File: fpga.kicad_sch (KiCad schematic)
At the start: 32 parts, among them J301 program, U301 ICE40HX8K-BG121, U302 W25Q32JVSS, Y301 50Mhz, Y302 12Mhz

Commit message: Working on board layout
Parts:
- D301: footprint LED_SMD:LED_1210_3225Metric -> LED_SMD:LED_1206_3216Metric
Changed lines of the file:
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@@
 			)
 		)
-		(property "Footprint" "LED_SMD:LED_1210_3225Metric"
+		(property "Footprint" "LED_SMD:LED_1206_3216Metric"
 			(at 210.82 66.04 0)
 			(effects

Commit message: More board layout
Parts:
- C301, C302, C303, C304, C305, C306, C307, C308, C309, C310, C311, C312, C313, C314, C315, C316, C317, C318: footprint Capacitor_SMD:C_0805_2012Metric -> Capacitor_SMD:C_0603_1608Metric
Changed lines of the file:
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@@
 			)
 		)
-		(property "Footprint" "Capacitor_SMD:C_0805_2012Metric"
+		(property "Footprint" "Capacitor_SMD:C_0603_1608Metric"
 			(at 40.9448 173.99 0)
 			(effects
@@
 			)
 		)
-		(property "Footprint" "Capacitor_SMD:C_0805_2012Metric"
+		(property "Footprint" "Capacitor_SMD:C_0603_1608Metric"
 			(at 240.3348 146.05 0)
 			(effects
@@
 			)
 		)
-		(property "Footprint" "Capacitor_SMD:C_0805_2012Metric"
+		(property "Footprint" "Capacitor_SMD:C_0603_1608Metric"
 			(at 193.3448 146.05 0)
 			(effects
@@
 			)
 		)
-		(property "Footprint" "Capacitor_SMD:C_0805_2012Metric"
+		(property "Footprint" "Capacitor_SMD:C_0603_1608Metric"
 			(at 72.6948 34.29 0)
 			(effects
@@
 			)
 		)
-		(property "Footprint" "Capacitor_SMD:C_0805_2012Metric"
+		(property "Footprint" "Capacitor_SMD:C_0603_1608Metric"
 			(at 100.6348 148.59 0)
 			(effects
@@
 			)
 		)
-		(property "Footprint" "Capacitor_SMD:C_0805_2012Metric"
+		(property "Footprint" "Capacitor_SMD:C_0603_1608Metric"
 			(at 108.2548 148.59 0)
 			(effects
@@
 			)
 		)
-		(property "Footprint" "Capacitor_SMD:C_0805_2012Metric"
+		(property "Footprint" "Capacitor_SMD:C_0603_1608Metric"
 			(at 216.2048 27.94 0)
 			(effects
@@
 			)
 		)
-		(property "Footprint" "Capacitor_SMD:C_0805_2012Metric"
+		(property "Footprint" "Capacitor_SMD:C_0603_1608Metric"
 			(at 208.5848 27.94 0)
 			(effects
@@
 			)
 		)
-		(property "Footprint" "Capacitor_SMD:C_0805_2012Metric"
+		(property "Footprint" "Capacitor_SMD:C_0603_1608Metric"
 			(at 80.3148 34.29 0)
 			(effects
@@
 			)
 		)
-		(property "Footprint" "Capacitor_SMD:C_0805_2012Metric"
+		(property "Footprint" "Capacitor_SMD:C_0603_1608Metric"
 			(at 132.3848 34.29 0)
 			(effects
@@
 			)
 		)
-		(property "Footprint" "Capacitor_SMD:C_0805_2012Metric"
+		(property "Footprint" "Capacitor_SMD:C_0603_1608Metric"
 			(at 273.3548 34.29 0)
 			(effects
@@
 			)
 		)
-		(property "Footprint" "Capacitor_SMD:C_0805_2012Metric"
+		(property "Footprint" "Capacitor_SMD:C_0603_1608Metric"
 			(at 48.5648 140.97 0)
 			(effects
@@
 			)
 		)
-		(property "Footprint" "Capacitor_SMD:C_0805_2012Metric"
+		(property "Footprint" "Capacitor_SMD:C_0603_1608Metric"
 			(at 168.6052 173.99 0)
 			(effects
@@
 			)
 		)
-		(property "Footprint" "Capacitor_SMD:C_0805_2012Metric"
+		(property "Footprint" "Capacitor_SMD:C_0603_1608Metric"
 			(at 40.9448 140.97 0)
 			(effects
@@
 			)
 		)
-		(property "Footprint" "Capacitor_SMD:C_0805_2012Metric"
+		(property "Footprint" "Capacitor_SMD:C_0603_1608Metric"
 			(at 48.5648 173.99 0)
 			(effects
@@
 			)
 		)
-		(property "Footprint" "Capacitor_SMD:C_0805_2012Metric"
+		(property "Footprint" "Capacitor_SMD:C_0603_1608Metric"
 			(at 93.0148 148.59 0)
 			(effects
@@
 			)
 		)
-		(property "Footprint" "Capacitor_SMD:C_0805_2012Metric"
+		(property "Footprint" "Capacitor_SMD:C_0603_1608Metric"
 			(at 280.9748 34.29 0)
 			(effects
@@
 			)
 		)
-		(property "Footprint" "Capacitor_SMD:C_0805_2012Metric"
+		(property "Footprint" "Capacitor_SMD:C_0603_1608Metric"
 			(at 140.0048 34.29 0)
 			(effects

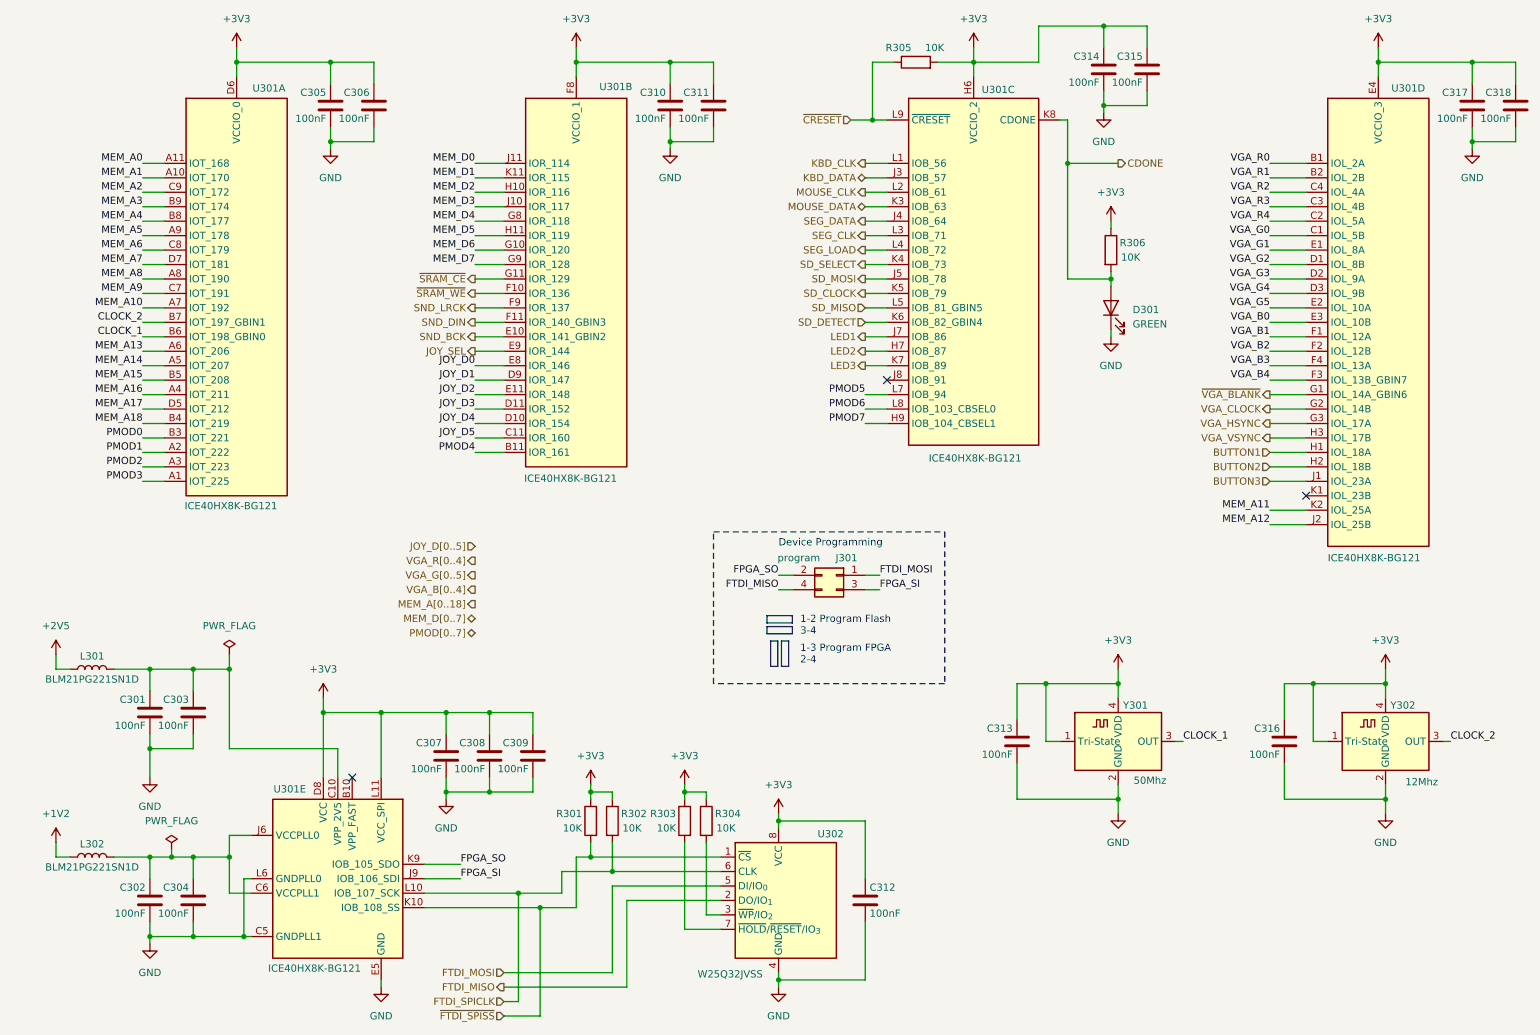
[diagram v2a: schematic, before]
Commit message: Started FPGA fanout
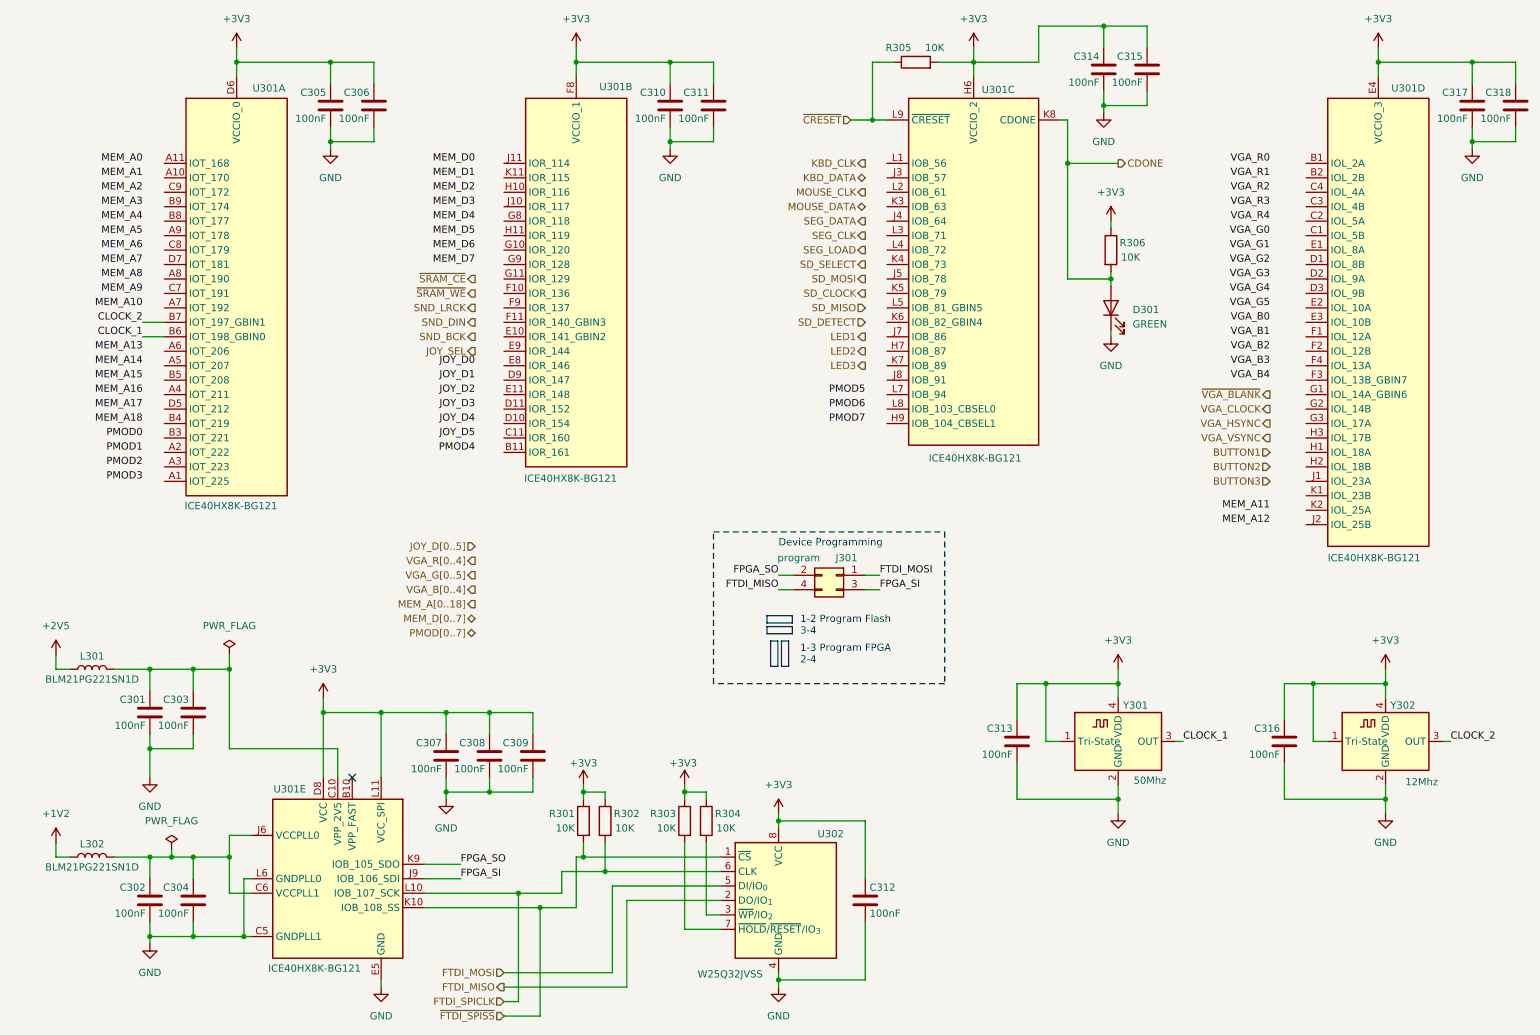
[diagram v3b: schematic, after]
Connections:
- net BUTTON1: no longer U301.H1 (IOL_18A)
- net BUTTON2: no longer U301.H2 (IOL_18B)
- net BUTTON3: no longer U301.J1 (IOL_23A)
- net JOY_D0: no longer U301.E8 (IOR_146)
- net JOY_D1: no longer U301.D9 (IOR_147)
- net JOY_D2: no longer U301.E11 (IOR_148)
- net JOY_D3: no longer U301.D11 (IOR_152)
- net JOY_D4: no longer U301.D10 (IOR_154)
- net JOY_D5: no longer U301.C11 (IOR_160)
- net JOY_SEL: no longer U301.E9 (IOR_144)
- net KBD_CLK: no longer U301.L1 (IOB_56)
- net KBD_DATA: no longer U301.J3 (IOB_57)
- net LED1: no longer U301.J7 (IOB_86)
- net LED2: no longer U301.H7 (IOB_87)
- net LED3: no longer U301.K7 (IOB_89)
- net MEM_A0: no longer U301.A11 (IOT_168)
- net MEM_A1: no longer U301.A10 (IOT_170)
- net MEM_A10: no longer U301.A7 (IOT_192)
- net MEM_A11: no longer U301.K2 (IOL_25A)
- net MEM_A12: no longer U301.J2 (IOL_25B)
- net MEM_A13: no longer U301.A6 (IOT_206)
- net MEM_A14: no longer U301.A5 (IOT_207)
- net MEM_A15: no longer U301.B5 (IOT_208)
- net MEM_A16: no longer U301.A4 (IOT_211)
- net MEM_A17: no longer U301.D5 (IOT_212)
- net MEM_A18: no longer U301.B4 (IOT_219)
- net MEM_A2: no longer U301.C9 (IOT_172)
- net MEM_A3: no longer U301.B9 (IOT_174)
- net MEM_A4: no longer U301.B8 (IOT_177)
- net MEM_A5: no longer U301.A9 (IOT_178)
- net MEM_A6: no longer U301.C8 (IOT_179)
- net MEM_A7: no longer U301.D7 (IOT_181)
- net MEM_A8: no longer U301.A8 (IOT_190)
- net MEM_A9: no longer U301.C7 (IOT_191)
- net MEM_D0: no longer U301.J11 (IOR_114)
- net MEM_D1: no longer U301.K11 (IOR_115)
- net MEM_D2: no longer U301.H10 (IOR_116)
- net MEM_D3: no longer U301.J10 (IOR_117)
- net MEM_D4: no longer U301.G8 (IOR_118)
- net MEM_D5: no longer U301.H11 (IOR_119)
- net MEM_D6: no longer U301.G10 (IOR_120)
- net MEM_D7: no longer U301.G9 (IOR_128)
- net MOUSE_CLK: no longer U301.L2 (IOB_61)
- net MOUSE_DATA: no longer U301.K3 (IOB_63)
- net PMOD0: no longer U301.B3 (IOT_221)
- net PMOD1: no longer U301.A2 (IOT_222)
- net PMOD2: no longer U301.A3 (IOT_223)
- net PMOD3: no longer U301.A1 (IOT_225)
- net PMOD4: no longer U301.B11 (IOR_161)
- net PMOD5: no longer U301.L7 (IOB_94)
- net PMOD6: no longer U301.L8 (IOB_103_CBSEL0)
- net PMOD7: no longer U301.H9 (IOB_104_CBSEL1)
- net SD_CLOCK: no longer U301.K5 (IOB_79)
- net SD_DETECT: no longer U301.K6 (IOB_82_GBIN4)
- net SD_MISO: no longer U301.L5 (IOB_81_GBIN5)
- net SD_MOSI: no longer U301.J5 (IOB_78)
- net SD_SELECT: no longer U301.K4 (IOB_73)
- net SEG_CLK: no longer U301.L3 (IOB_71)
- net SEG_DATA: no longer U301.J4 (IOB_64)
- net SEG_LOAD: no longer U301.L4 (IOB_72)
- net SND_BCK: no longer U301.E10 (IOR_141_GBIN2)
- net SND_DIN: no longer U301.F11 (IOR_140_GBIN3)
- net SND_LRCK: no longer U301.F9 (IOR_137)
- net VGA_B0: no longer U301.E3 (IOL_10B)
- net VGA_B1: no longer U301.F1 (IOL_12A)
- net VGA_B2: no longer U301.F2 (IOL_12B)
- net VGA_B3: no longer U301.F4 (IOL_13A)
- net VGA_B4: no longer U301.F3 (IOL_13B_GBIN7)
- net VGA_CLOCK: no longer U301.G2 (IOL_14B)
- net VGA_G0: no longer U301.C1 (IOL_5B)
- net VGA_G1: no longer U301.E1 (IOL_8A)
- net VGA_G2: no longer U301.D1 (IOL_8B)
- net VGA_G3: no longer U301.D2 (IOL_9A)
- net VGA_G4: no longer U301.D3 (IOL_9B)
- net VGA_G5: no longer U301.E2 (IOL_10A)
- net VGA_HSYNC: no longer U301.G3 (IOL_17A)
- net VGA_R0: no longer U301.B1 (IOL_2A)
- net VGA_R1: no longer U301.B2 (IOL_2B)
- net VGA_R2: no longer U301.C4 (IOL_4A)
- net VGA_R3: no longer U301.C3 (IOL_4B)
- net VGA_R4: no longer U301.C2 (IOL_5A)
- net VGA_VSYNC: no longer U301.H3 (IOL_17B)
- net ~{SRAM_CE}: no longer U301.G11 (IOR_129)
- net ~{SRAM_WE}: no longer U301.F10 (IOR_136)
- net ~{VGA_BLANK}: no longer U301.G1 (IOL_14A_GBIN6)
- no-connect marks 3 -> 1
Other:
- moved on the sheet: R301, R302

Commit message: Initial FPGA layout done
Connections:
- net BUTTON1: now also U301.K5 (IOB_79)
- net BUTTON2: now also U301.L5 (IOB_81_GBIN5)
- net BUTTON3: now also U301.K6 (IOB_82_GBIN4)
- net JOY_D0: now also U301.A6 (IOT_206)
- net JOY_D1: now also U301.A7 (IOT_192)
- net JOY_D2: now also U301.D7 (IOT_181)
- net JOY_D3: now also U301.B8 (IOT_177)
- net JOY_D4: now also U301.A8 (IOT_190)
- net JOY_D5: now also U301.C7 (IOT_191)
- net JOY_SEL: now also U301.A5 (IOT_207)
- net KBD_CLK: now also U301.A9 (IOT_178)
- net KBD_DATA: now also U301.B9 (IOT_174)
- net LED1: now also U301.L4 (IOB_72)
- net LED2: now also U301.K4 (IOB_73)
- net LED3: now also U301.J5 (IOB_78)
- net MEM_A0: now also U301.L2 (IOB_61)
- net MEM_A1: now also U301.L1 (IOB_56)
- net MEM_A10: now also U301.A1 (IOT_225)
- net MEM_A11: now also U301.A2 (IOT_222)
- net MEM_A12: now also U301.B2 (IOL_2B)
- net MEM_A13: now also U301.B1 (IOL_2A)
- net MEM_A14: now also U301.C2 (IOL_5A)
- net MEM_A15: now also U301.E2 (IOL_10A)
- net MEM_A16: now also U301.E3 (IOL_10B)
- net MEM_A17: now also U301.E1 (IOL_8A)
- net MEM_A18: now also U301.F3 (IOL_13B_GBIN7)
- net MEM_A2: now also U301.K2 (IOL_25A)
- net MEM_A3: now also U301.K1 (IOL_23B)
- net MEM_A4: now also U301.J2 (IOL_25B)
- net MEM_A5: now also U301.G2 (IOL_14B)
- net MEM_A6: now also U301.G3 (IOL_17A)
- net MEM_A7: now also U301.F1 (IOL_12A)
- net MEM_A8: now also U301.F4 (IOL_13A)
- net MEM_A9: now also U301.F2 (IOL_12B)
- net MEM_D0: now also U301.J3 (IOB_57)
- net MEM_D1: now also U301.H1 (IOL_18A)
- net MEM_D2: now also U301.H2 (IOL_18B)
- net MEM_D3: now also U301.H3 (IOL_17B)
- net MEM_D4: now also U301.C1 (IOL_5B)
- net MEM_D5: now also U301.D2 (IOL_9A)
- net MEM_D6: now also U301.D3 (IOL_9B)
- net MEM_D7: now also U301.D1 (IOL_8B)
- net MOUSE_CLK: now also U301.C9 (IOT_172)
- net MOUSE_DATA: now also U301.A10 (IOT_170)
- net PMOD0: now also U301.B5 (IOT_208)
- net PMOD1: now also U301.A4 (IOT_211)
- net PMOD2: now also U301.C4 (IOL_4A)
- net PMOD3: now also U301.B3 (IOT_221)
- net PMOD4: now also U301.D5 (IOT_212)
- net PMOD5: now also U301.B4 (IOT_219)
- net PMOD6: now also U301.A3 (IOT_223)
- net PMOD7: now also U301.C3 (IOL_4B)
- net SD_CLOCK: now also U301.C11 (IOR_160)
- net SD_DETECT: now also U301.D9 (IOR_147)
- net SD_MISO: now also U301.D10 (IOR_154)
- net SD_MOSI: now also U301.B11 (IOR_161)
- net SD_SELECT: now also U301.A11 (IOT_168)
- net SEG_CLK: now also U301.J4 (IOB_64)
- net SEG_DATA: now also U301.K3 (IOB_63)
- net SEG_LOAD: now also U301.L3 (IOB_71)
- net SND_BCK: now also U301.D11 (IOR_152)
- net SND_DIN: now also U301.E9 (IOR_144)
- net SND_LRCK: now also U301.E10 (IOR_141_GBIN2)
- net VGA_B0: now also U301.H10 (IOR_116)
- net VGA_B1: now also U301.J11 (IOR_114)
- net VGA_B2: now also U301.H9 (IOB_104_CBSEL1)
- net VGA_B3: now also U301.K11 (IOR_115)
- net VGA_B4: now also U301.J10 (IOR_117)
- net VGA_CLOCK: now also U301.F11 (IOR_140_GBIN3)
- net VGA_G0: now also U301.K7 (IOB_89)
- net VGA_G1: now also U301.J7 (IOB_86)
- net VGA_G2: now also U301.L7 (IOB_94)
- net VGA_G3: now also U301.H7 (IOB_87)
- net VGA_G4: now also U301.L8 (IOB_103_CBSEL0)
- net VGA_G5: now also U301.J8 (IOB_91)
- net VGA_HSYNC: now also U301.F10 (IOR_136)
- net VGA_R0: now also U301.G10 (IOR_120)
- net VGA_R1: now also U301.G11 (IOR_129)
- net VGA_R2: now also U301.E8 (IOR_146)
- net VGA_R3: now also U301.G8 (IOR_118)
- net VGA_R4: now also U301.H11 (IOR_119)
- net VGA_VSYNC: now also U301.F9 (IOR_137)
- net ~{SRAM_CE}: now also U301.J1 (IOL_23A)
- net ~{SRAM_WE}: now also U301.G1 (IOL_14A_GBIN6)
- net ~{VGA_BLANK}: now also U301.E11 (IOR_148)

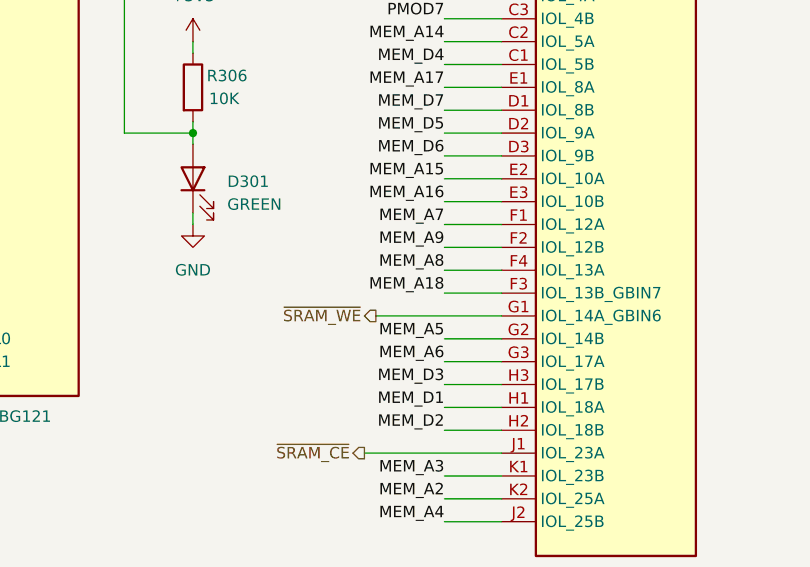
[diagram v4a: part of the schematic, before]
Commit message: Started board routing
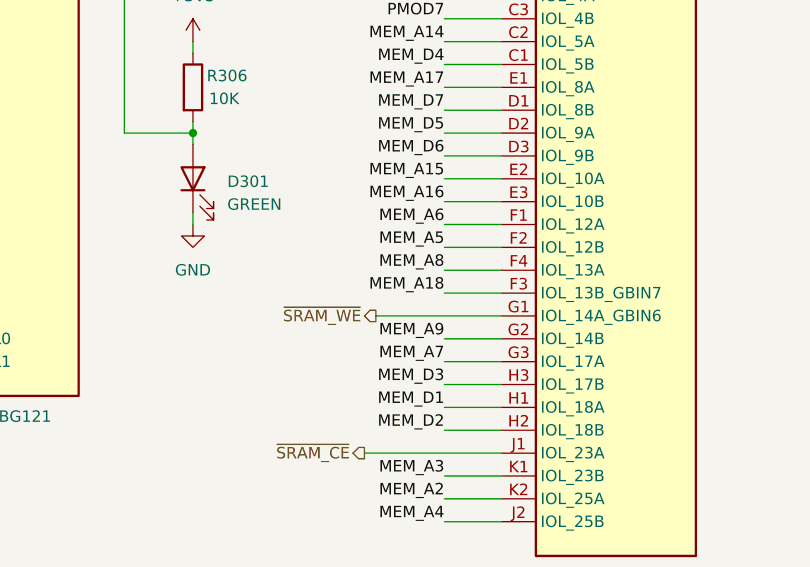
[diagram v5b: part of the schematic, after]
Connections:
- net MEM_A5: now also U301.F2 (IOL_12B); no longer U301.G2 (IOL_14B)
- net MEM_A6: now also U301.F1 (IOL_12A); no longer U301.G3 (IOL_17A)
- net MEM_A7: now also U301.G3 (IOL_17A); no longer U301.F1 (IOL_12A)
- net MEM_A9: now also U301.G2 (IOL_14B); no longer U301.F2 (IOL_12B)
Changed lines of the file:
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@@
 	)
 	(label "MEM_A7"
-		(at 238.76 71.12 180)
+		(at 238.76 86.36 180)
 		(effects
 			(font
@@
 	)
 	(label "MEM_A6"
-		(at 238.76 86.36 180)
+		(at 238.76 71.12 180)
 		(effects
 			(font
@@
 	)
 	(label "MEM_A5"
-		(at 238.76 83.82 180)
+		(at 238.76 73.66 180)
 		(effects
 			(font
@@
 	)
 	(label "MEM_A9"
-		(at 238.76 73.66 180)
-		(effects
-			(font
+		(at 238.76 83.82 180)
+		(effects
+			(font

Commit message: Routed SRAM
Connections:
- net MEM_A10: now also U301.A2 (IOT_222); no longer U301.A1 (IOT_225)
- net MEM_A11: now also U301.A1 (IOT_225); no longer U301.A2 (IOT_222)
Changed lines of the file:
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@@
 	)
 	(label "MEM_A11"
-		(at 39.37 91.44 180)
+		(at 39.37 96.52 180)
 		(effects
 			(font
@@
 	)
 	(label "MEM_A10"
-		(at 39.37 96.52 180)
+		(at 39.37 91.44 180)
 		(effects
 			(font
